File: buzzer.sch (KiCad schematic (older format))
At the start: 4 parts, among them Q1 NPN, U7 CSS-0575A-SMT

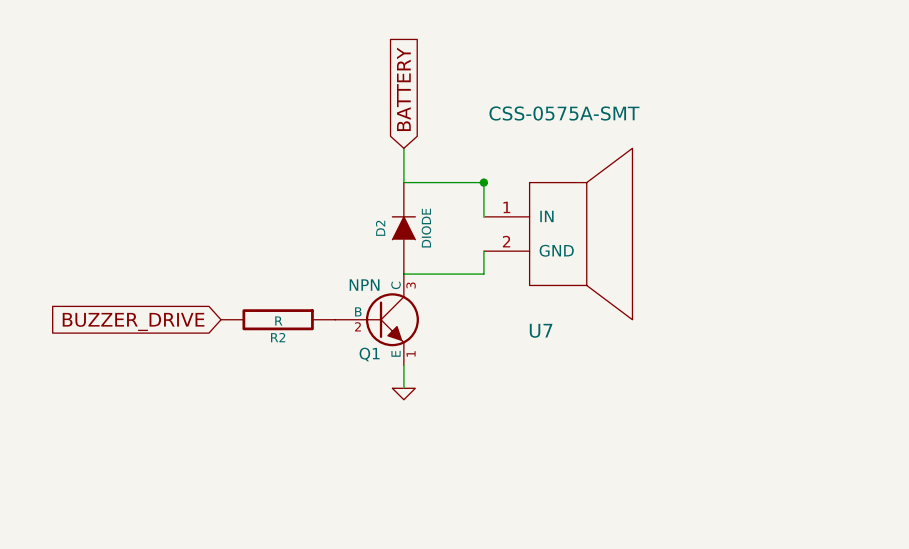
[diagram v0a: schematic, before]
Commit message: Add gps
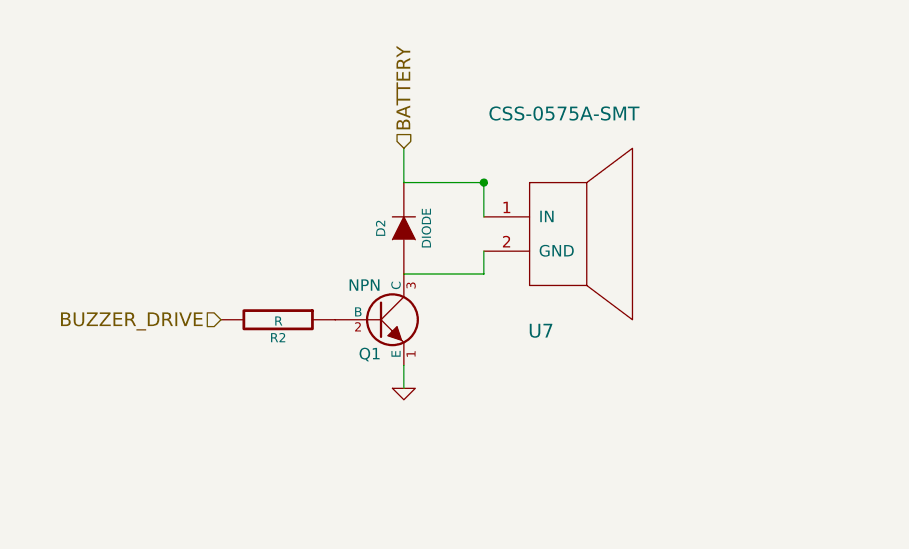
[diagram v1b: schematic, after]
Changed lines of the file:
@@
 $Descr A4 11693 8268
 encoding utf-8
-Sheet 8 10
+Sheet 8 11
 Title ""
 Date ""
@@
 $EndComp
 $Comp
-L GND #PWR12
+L GND #PWR18
 U 1 1 54464591
 P 5450 3950
-F 0 "#PWR12" H 5450 3950 30  0001 C CNN
+F 0 "#PWR18" H 5450 3950 30  0001 C CNN
 F 1 "GND" H 5450 3880 30  0001 C CNN
 F 2 "" H 5450 3950 60  0000 C CNN
@@
 	1    0    0    -1
 $EndComp
-Text GLabel 5450 2900 1    60   Input ~ 0
-BATTERY
-Text GLabel 4650 3650 0    60   Input ~ 0
-BUZZER_DRIVE
 Wire Wire Line
 	5800 3350 5800 3450
@@
 Wire Wire Line
 	5450 3050 5450 2900
+Text HLabel 5450 2900 1    60   Input ~ 0
+BATTERY
+Text HLabel 4650 3650 0    60   Input ~ 0
+BUZZER_DRIVE
 $EndSCHEMATC

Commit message: More connections
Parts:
- D2, R2: footprint (none) -> buq2:SM0603
- Q1: footprint (none) -> buq2:SOT-23-3
- U7: footprint (none) -> buq2:BUZZER-CUI-5MM
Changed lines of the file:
@@
 F 0 "U7" H 6050 3600 60  0000 C CNN
 F 1 "CSS-0575A-SMT" H 6150 4550 60  0000 C CNN
-F 2 "" H 5800 3650 60  0001 C CNN
+F 2 "buq2:BUZZER-CUI-5MM" H 5800 3650 60  0001 C CNN
 F 3 "" H 5800 3650 60  0000 C CNN
 	1    5800 3650
@@
 F 0 "Q1" H 5350 3500 50  0000 R CNN
 F 1 "NPN" H 5350 3800 50  0000 R CNN
-F 2 "" H 5350 3650 60  0001 C CNN
+F 2 "buq2:SOT-23-3" H 5350 3650 60  0001 C CNN
 F 3 "" H 5350 3650 60  0000 C CNN
 	1    5350 3650
@@
 F 0 "R2" V 4980 3650 40  0000 C CNN
 F 1 "R" V 4907 3651 40  0000 C CNN
-F 2 "" V 4830 3650 30  0001 C CNN
+F 2 "buq2:SM0603" V 4830 3650 30  0001 C CNN
 F 3 "" H 4900 3650 30  0000 C CNN
 	1    4900 3650
@@
 F 0 "D2" H 5450 3350 40  0000 C CNN
 F 1 "DIODE" H 5450 3150 40  0000 C CNN
-F 2 "" H 5450 3250 60  0001 C CNN
+F 2 "buq2:SM0603" H 5450 3250 60  0001 C CNN
 F 3 "" H 5450 3250 60  0000 C CNN
 	1    5450 3250
@@
 $EndComp
 $Comp
-L GND #PWR18
+L GND #PWR020
 U 1 1 54464591
 P 5450 3950
-F 0 "#PWR18" H 5450 3950 30  0001 C CNN
+F 0 "#PWR020" H 5450 3950 30  0001 C CNN
 F 1 "GND" H 5450 3880 30  0001 C CNN
 F 2 "" H 5450 3950 60  0000 C CNN

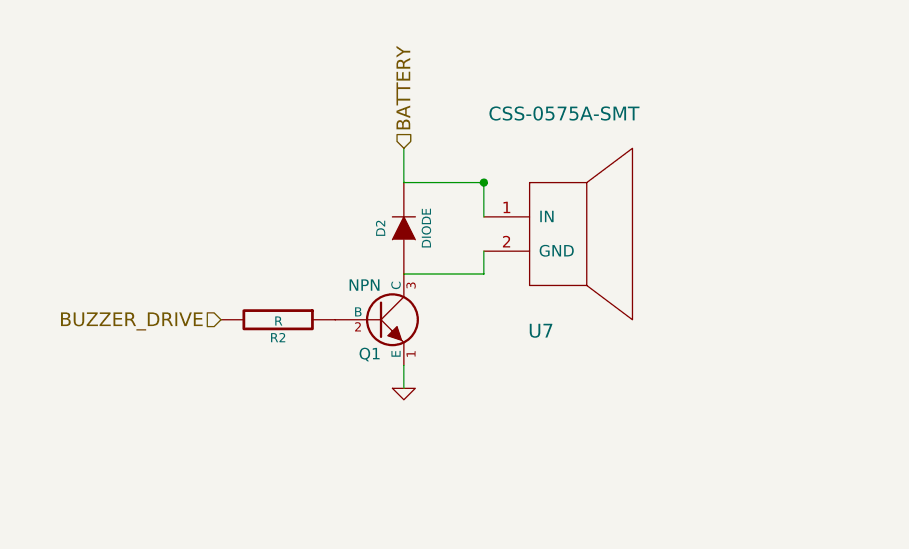
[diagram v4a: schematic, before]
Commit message: Add buttons. Fix DRC. Add antenna
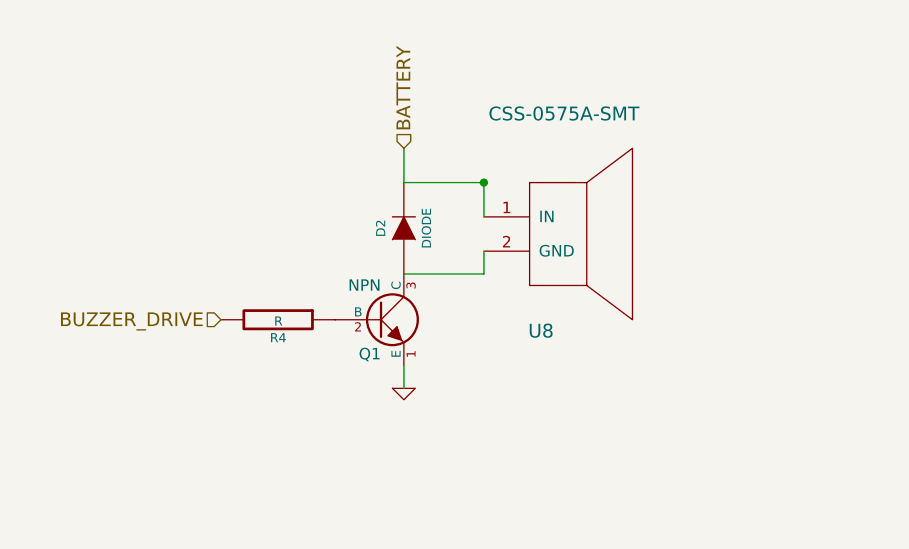
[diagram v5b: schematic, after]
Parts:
- renumbered R2 to R4, U7 to U8
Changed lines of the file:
@@
 $Descr A4 11693 8268
 encoding utf-8
-Sheet 8 13
+Sheet 8 14
 Title ""
 Date ""
@@
 $EndDescr
 $Comp
-L CSS-0575A-SMT U7
+L CSS-0575A-SMT U8
 U 1 1 54464575
 P 5800 3650
-F 0 "U7" H 6050 3600 60  0000 C CNN
+F 0 "U8" H 6050 3600 60  0000 C CNN
 F 1 "CSS-0575A-SMT" H 6150 4550 60  0000 C CNN
 F 2 "buq2:BUZZER-CUI-5MM" H 5800 3650 60  0001 C CNN
@@
 $EndComp
 $Comp
-L R R2
+L R R4
 U 1 1 54464583
 P 4900 3650
-F 0 "R2" V 4980 3650 40  0000 C CNN
+F 0 "R4" V 4980 3650 40  0000 C CNN
 F 1 "R" V 4907 3651 40  0000 C CNN
 F 2 "buq2:SM0603" V 4830 3650 30  0001 C CNN
@@
 $EndComp
 $Comp
-L GND #PWR021
+L GND #PWR024
 U 1 1 54464591
 P 5450 3950
-F 0 "#PWR021" H 5450 3950 30  0001 C CNN
+F 0 "#PWR024" H 5450 3950 30  0001 C CNN
 F 1 "GND" H 5450 3880 30  0001 C CNN
 F 2 "" H 5450 3950 60  0000 C CNN

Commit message: Start planning test board v2.0
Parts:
- added R7, R8: 25, buq2:SM0603, symbol R
- R4: value R -> 1k
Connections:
- net BATTERY: now also R7.2; no longer U8.1 (IN)
- new net: R8.1, U8.1 (IN)
- new net: R7.1, R8.2
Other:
- note added: "two 0603 resistors as\npower dissipation is 0.2w"
- moved on the sheet: U8
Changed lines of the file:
@@
 $Descr A4 11693 8268
 encoding utf-8
-Sheet 8 14
+Sheet 7 10
 Title ""
 Date ""
@@
 L CSS-0575A-SMT U8
 U 1 1 54464575
-P 5800 3650
-F 0 "U8" H 6050 3600 60  0000 C CNN
-F 1 "CSS-0575A-SMT" H 6150 4550 60  0000 C CNN
-F 2 "buq2:BUZZER-CUI-5MM" H 5800 3650 60  0001 C CNN
-F 3 "" H 5800 3650 60  0000 C CNN
-	1    5800 3650
+P 6800 3650
+F 0 "U8" H 7050 3600 60  0000 C CNN
+F 1 "CSS-0575A-SMT" H 7150 4550 60  0000 C CNN
+F 2 "buq2:BUZZER-CUI-5MM" H 6800 3650 60  0001 C CNN
+F 3 "" H 6800 3650 60  0000 C CNN
+	1    6800 3650
 	1    0    0    -1
 $EndComp
@@
 P 4900 3650
 F 0 "R4" V 4980 3650 40  0000 C CNN
-F 1 "R" V 4907 3651 40  0000 C CNN
+F 1 "1k" V 4907 3651 40  0000 C CNN
 F 2 "buq2:SM0603" V 4830 3650 30  0001 C CNN
 F 3 "" H 4900 3650 30  0000 C CNN
@@
 Connection ~ 5800 3050
 Wire Wire Line
-	5800 3200 5800 3050
-Wire Wire Line
 	5450 3950 5450 3850
 Wire Wire Line
@@
 Text HLabel 4650 3650 0    60   Input ~ 0
 BUZZER_DRIVE
+$Comp
+L R R7
+U 1 1 54C74B42
+P 6050 3050
+F 0 "R7" V 6130 3050 40  0000 C CNN
+F 1 "25" V 6057 3051 40  0000 C CNN
+F 2 "buq2:SM0603" V 5980 3050 30  0001 C CNN
+F 3 "" H 6050 3050 30  0000 C CNN
+	1    6050 3050
+	0    1    1    0
+$EndComp
+Wire Wire Line
+	6800 3350 5800 3350
+$Comp
+L R R8
+U 1 1 54C74F1A
+P 6550 3050
+F 0 "R8" V 6630 3050 40  0000 C CNN
+F 1 "25" V 6557 3051 40  0000 C CNN
+F 2 "buq2:SM0603" V 6480 3050 30  0001 C CNN
+F 3 "" H 6550 3050 30  0000 C CNN
+	1    6550 3050
+	0    1    1    0
+$EndComp
+Wire Wire Line
+	6800 3050 6800 3200
+Text Notes 5650 2900 0    60   ~ 0
+two 0603 resistors as\npower dissipation is 0.2w
 $EndSCHEMATC

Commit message: Almost ready routing
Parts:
- added SP1: SPEAKER, buq2:SPEAKER_240326000031, symbol SPEAKER
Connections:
- net at R8.1, U8.1 (IN): now also SP1.1
- net at D2.1 (A), Q1.3 (C), U8.2 (GND): now also SP1.2
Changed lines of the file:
@@
 Text Notes 5650 2900 0    60   ~ 0
 two 0603 resistors as\npower dissipation is 0.2w
+$Comp
+L SPEAKER SP1
+U 1 1 54C7C4BE
+P 7250 4250
+F 0 "SP1" H 7150 4500 70  0000 C CNN
+F 1 "SPEAKER" H 7150 4000 70  0000 C CNN
+F 2 "buq2:SPEAKER_240326000031" H 7250 4250 60  0001 C CNN
+F 3 "http://media.digikey.com/pdf/Data%20Sheets/Knowles%20Acoustics%20PDFs/2403-260-00031.pdf" H 7250 4250 60  0001 C CNN
+	1    7250 4250
+	1    0    0    -1
+$EndComp
+Wire Wire Line
+	6800 3150 6650 3150
+Wire Wire Line
+	6650 3150 6650 4150
+Wire Wire Line
+	6650 4150 6950 4150
+Connection ~ 6800 3150
+Wire Wire Line
+	6750 3350 6750 4350
+Wire Wire Line
+	6750 4350 6950 4350
+Connection ~ 6750 3350
 $EndSCHEMATC
